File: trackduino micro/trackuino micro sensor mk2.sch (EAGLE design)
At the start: 42 parts, among them IC2 74AHC1G125DBV, SW1 SPST_TACT-KMR2, U1 ATMEGA168MLF, Y1 16MHZ

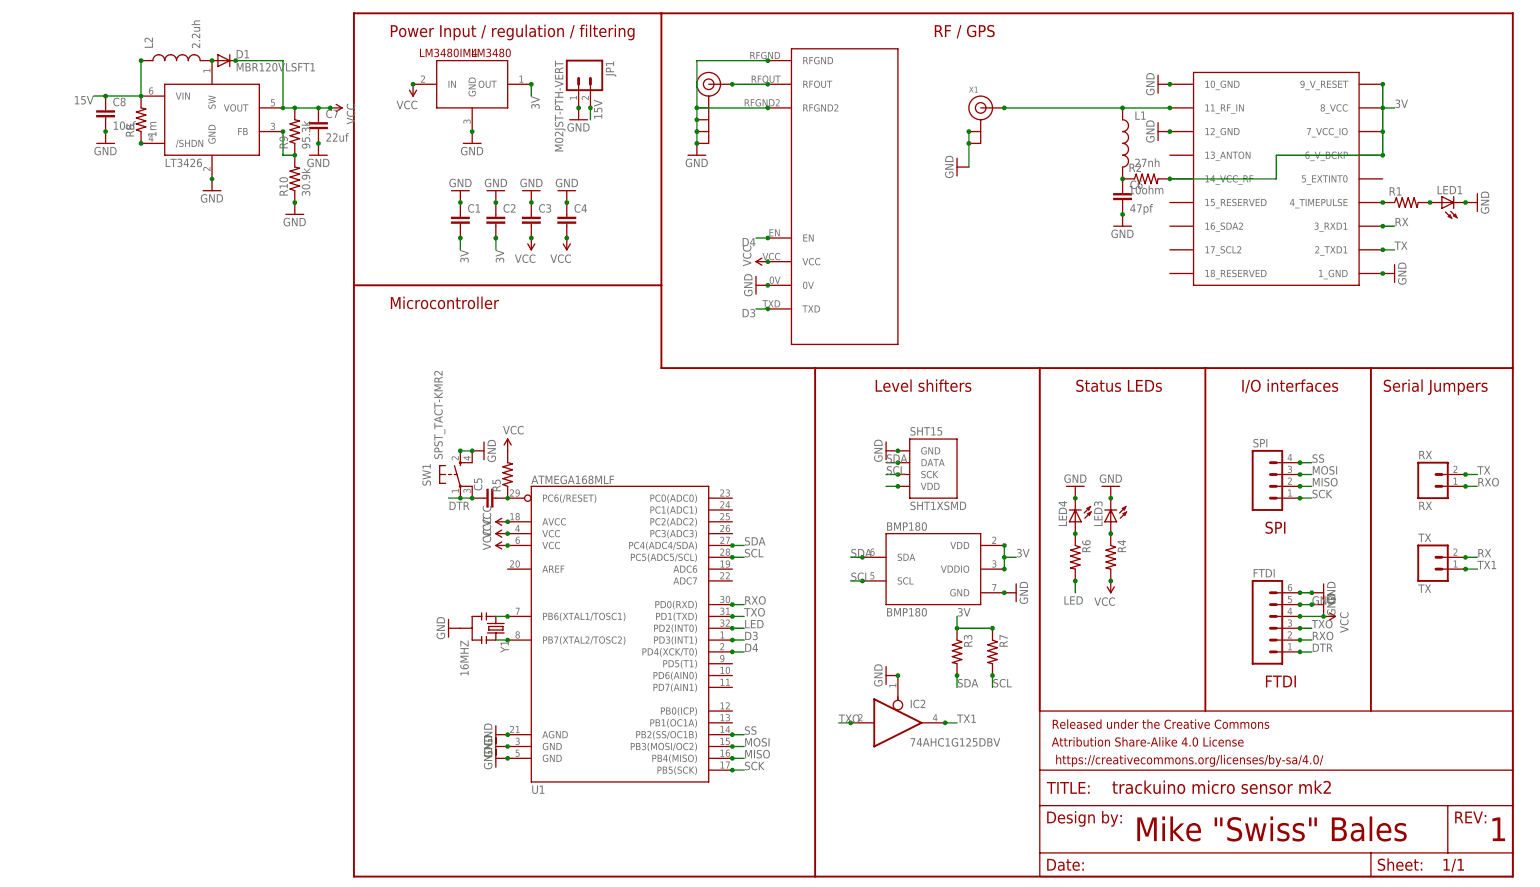
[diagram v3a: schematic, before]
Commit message: added part values
added part values to the schematic.
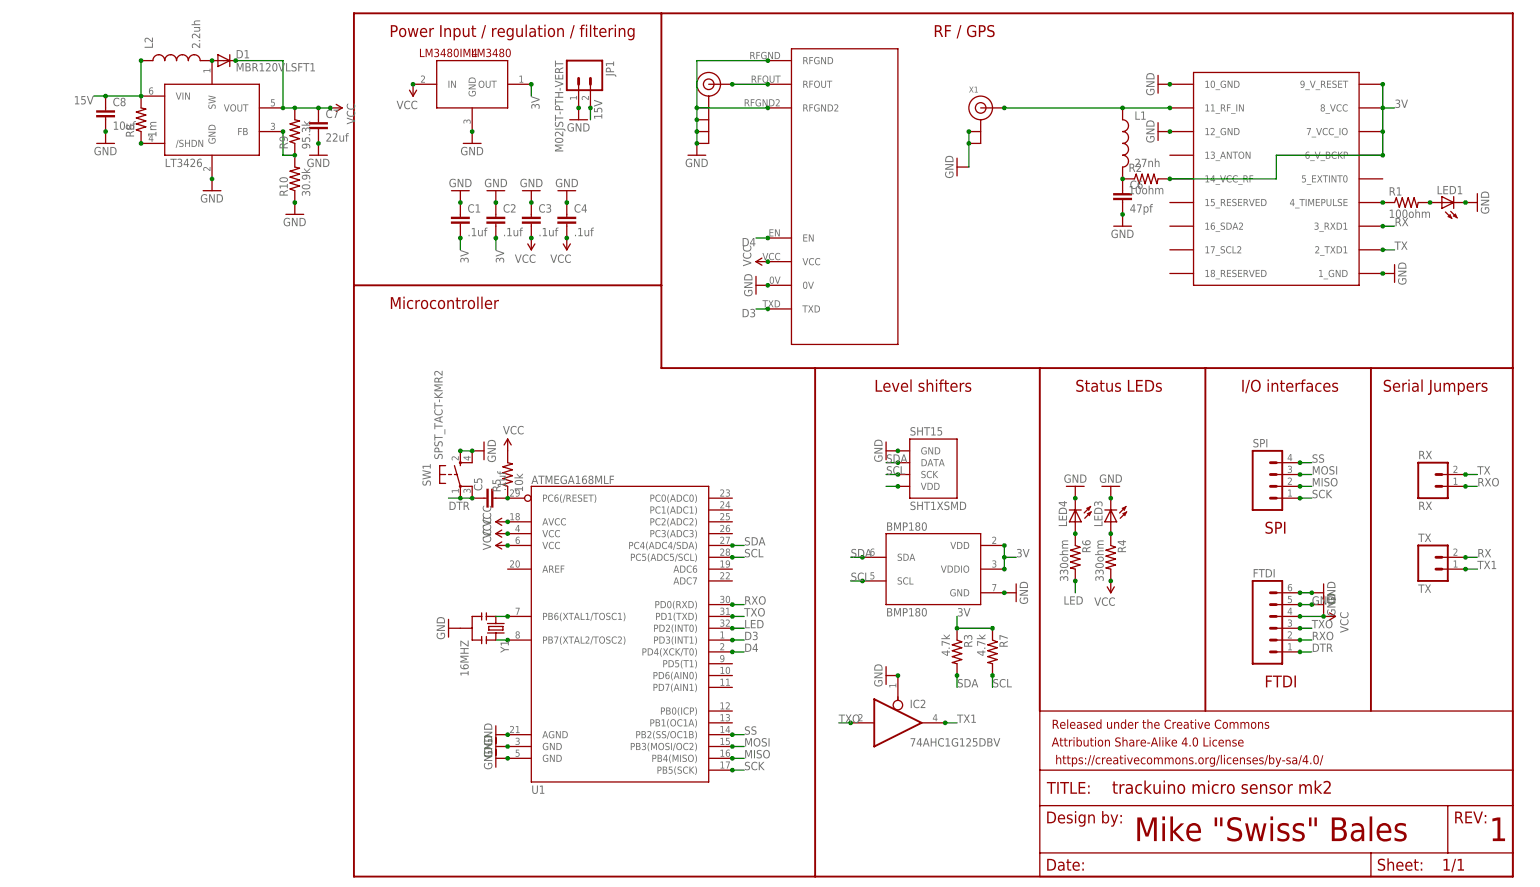
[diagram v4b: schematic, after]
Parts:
- C1, C2, C3, C4, C5: value (none) -> .1uf
- R1: value (none) -> 100ohm
- R3, R7: value (none) -> 4.7k
- R4, R6: value (none) -> 330ohm
- R5: value (none) -> 10k
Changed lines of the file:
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@@
 <part name="SUPPLY3" library="SparkFun-Aesthetics" deviceset="VCC" device=""/>
 <part name="GND7" library="SparkFun-Aesthetics" deviceset="GND" device=""/>
-<part name="R1" library="SparkFun-Resistors" deviceset="RESISTOR" device="0805-RES"/>
+<part name="R1" library="SparkFun-Resistors" deviceset="RESISTOR" device="0805-RES" value="100ohm"/>
 <part name="LED1" library="adafruit" deviceset="LED" device="CHIP-LED0805"/>
 <part name="GND8" library="SparkFun-Aesthetics" deviceset="GND" device=""/>
@@
 <part name="GND13" library="SparkFun-Aesthetics" deviceset="GND" device=""/>
 <part name="GND14" library="SparkFun-Aesthetics" deviceset="GND" device=""/>
-<part name="C1" library="SparkFun-Capacitors" deviceset="CAP" device="0805"/>
-<part name="C2" library="SparkFun-Capacitors" deviceset="CAP" device="0805"/>
-<part name="C3" library="SparkFun-Capacitors" deviceset="CAP" device="0805"/>
-<part name="C4" library="SparkFun-Capacitors" deviceset="CAP" device="0805"/>
+<part name="C1" library="SparkFun-Capacitors" deviceset="CAP" device="0805" value=".1uf"/>
+<part name="C2" library="SparkFun-Capacitors" deviceset="CAP" device="0805" value=".1uf"/>
+<part name="C3" library="SparkFun-Capacitors" deviceset="CAP" device="0805" value=".1uf"/>
+<part name="C4" library="SparkFun-Capacitors" deviceset="CAP" device="0805" value=".1uf"/>
 <part name="GND15" library="SparkFun-Aesthetics" deviceset="GND" device=""/>
 <part name="GND17" library="SparkFun-Aesthetics" deviceset="GND" device=""/>
@@
 <part name="SUPPLY5" library="SparkFun-Aesthetics" deviceset="VCC" device=""/>
 <part name="LED3" library="adafruit" deviceset="LED" device="CHIP-LED0805"/>
-<part name="R4" library="SparkFun-Resistors" deviceset="RESISTOR" device="0805-RES"/>
+<part name="R4" library="SparkFun-Resistors" deviceset="RESISTOR" device="0805-RES" value="330ohm"/>
 <part name="GND19" library="SparkFun-Aesthetics" deviceset="GND" device=""/>
 <part name="SUPPLY6" library="SparkFun-Aesthetics" deviceset="VCC" device=""/>
@@
 <part name="GND22" library="SparkFun-Aesthetics" deviceset="GND" device=""/>
 <part name="SUPPLY9" library="SparkFun-Aesthetics" deviceset="VCC" device=""/>
-<part name="R5" library="SparkFun-Resistors" deviceset="RESISTOR" device="0805-RES"/>
+<part name="R5" library="SparkFun-Resistors" deviceset="RESISTOR" device="0805-RES" value="10k"/>
 <part name="SUPPLY10" library="SparkFun-Aesthetics" deviceset="VCC" device=""/>
-<part name="C5" library="SparkFun-Capacitors" deviceset="CAP" device="0805"/>
+<part name="C5" library="SparkFun-Capacitors" deviceset="CAP" device="0805" value=".1uf"/>
 <part name="TX" library="SparkFun-Connectors" deviceset="M02" device="PTH" value="TX"/>
 <part name="SPI" library="SparkFun-Connectors" deviceset="M04" device="1X04_NO_SILK"/>
@@
 <part name="GND25" library="SparkFun-Aesthetics" deviceset="GND" device=""/>
 <part name="LED4" library="adafruit" deviceset="LED" device="CHIP-LED0805"/>
-<part name="R6" library="SparkFun-Resistors" deviceset="RESISTOR" device="0805-RES"/>
+<part name="R6" library="SparkFun-Resistors" deviceset="RESISTOR" device="0805-RES" value="330ohm"/>
 <part name="GND26" library="SparkFun-Aesthetics" deviceset="GND" device=""/>
 <part name="GND24" library="SparkFun-Aesthetics" deviceset="GND" device=""/>
@@
 <part name="GND16" library="SparkFun-Aesthetics" deviceset="GND" device=""/>
 <part name="GND20" library="SparkFun-Aesthetics" deviceset="GND" device=""/>
-<part name="R3" library="SparkFun-Resistors" deviceset="RESISTOR" device="0805-RES"/>
-<part name="R7" library="SparkFun-Resistors" deviceset="RESISTOR" device="0805-RES"/>
+<part name="R3" library="SparkFun-Resistors" deviceset="RESISTOR" device="0805-RES" value="4.7k"/>
+<part name="R7" library="SparkFun-Resistors" deviceset="RESISTOR" device="0805-RES" value="4.7k"/>
 <part name="GND27" library="SparkFun-Aesthetics" deviceset="GND" device=""/>
 <part name="SUPPLY1" library="SparkFun-Aesthetics" deviceset="VCC" device=""/>

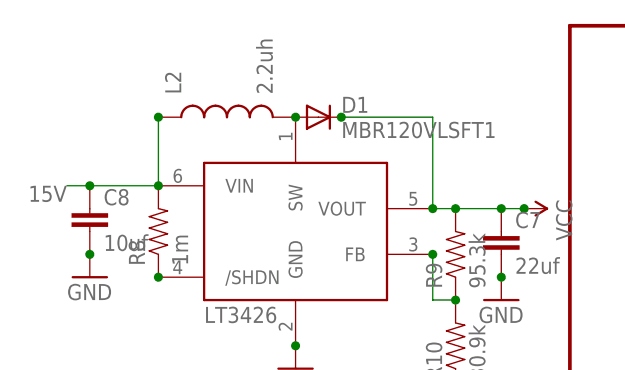
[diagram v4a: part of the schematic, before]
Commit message: replaced inductor
the 0805 inductor was getting way too hot due to being run well beyond
saturation. replaced with a 1812 inductor
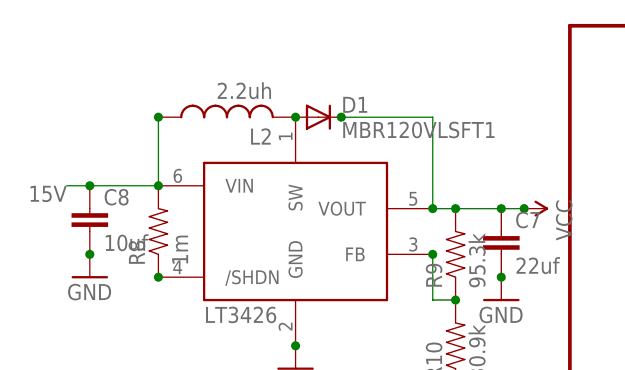
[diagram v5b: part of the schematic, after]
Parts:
- L2: device SparkFun-Passives:INDUCTOR0805 -> resistor:L-USL1812
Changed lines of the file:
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@@
 <?xml version="1.0" encoding="utf-8"?>
 <!DOCTYPE eagle SYSTEM "eagle.dtd">
-<eagle version="7.1.0">
+<eagle version="7.2.0">
 <drawing>
 <settings>
@@
 <part name="LT3426" library="adafruit" deviceset="LT3426" device=""/>
 <part name="D1" library="diode" deviceset="DIODE-" device="SOD123" value="MBR120VLSFT1"/>
-<part name="L2" library="SparkFun-Passives" deviceset="INDUCTOR" device="0805" value="2.2uh"/>
+<part name="L2" library="resistor" deviceset="L-US" device="L1812" value="2.2uh"/>
 <part name="R8" library="SparkFun-Resistors" deviceset="RESISTOR" device="0805-RES" value="1m"/>
 <part name="R9" library="SparkFun-Resistors" deviceset="RESISTOR" device="0805-RES" value="95.3k"/>

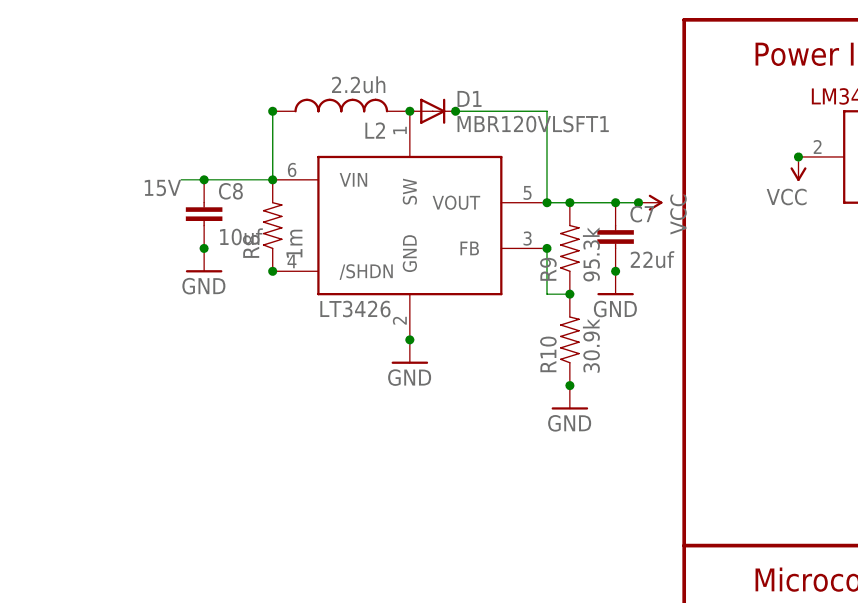
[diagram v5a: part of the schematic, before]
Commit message: added output cap
added a larger value output cap
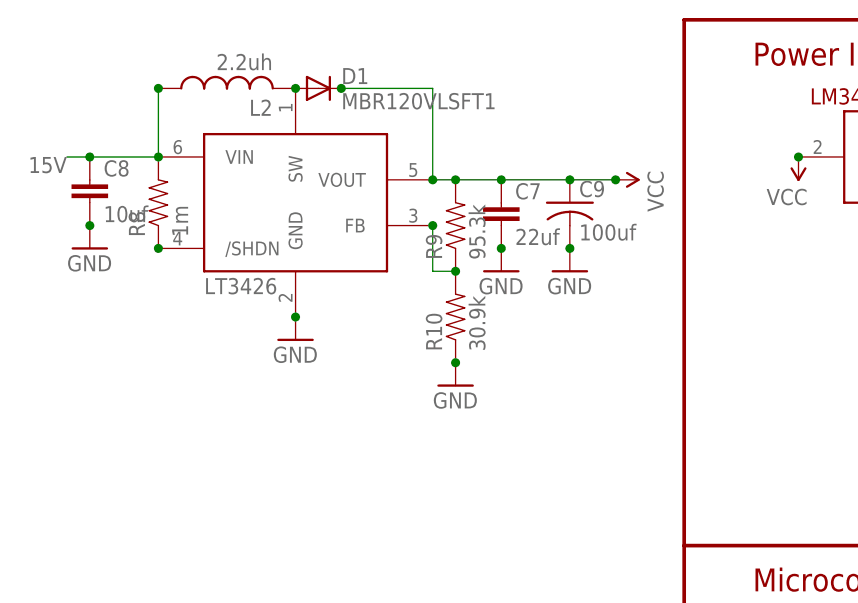
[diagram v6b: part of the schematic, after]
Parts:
- added C9: 100uf, resistor:C-USC1206
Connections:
- net GND: now also C9.2
- net VCC: now also C9.1
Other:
- moved on the sheet: C7, C8, D1, L2, R10, R8, R9
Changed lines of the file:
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@@
 <part name="GND29" library="SparkFun-Aesthetics" deviceset="GND" device=""/>
 <part name="GND30" library="SparkFun-Aesthetics" deviceset="GND" device=""/>
+<part name="C9" library="resistor" deviceset="C-US" device="C1206" value="100uf"/>
+<part name="GND31" library="SparkFun-Aesthetics" deviceset="GND" device=""/>
 </parts>
 <sheets>
@@
 <instance part="R3" gate="G$1" x="129.54" y="48.26" rot="R270"/>
 <instance part="R7" gate="G$1" x="137.16" y="48.26" rot="R270"/>
-<instance part="GND27" gate="1" x="-30.48" y="147.32"/>
-<instance part="SUPPLY1" gate="G$1" x="-5.08" y="165.1" rot="R270"/>
-<instance part="LT3426" gate="G$1" x="-30.48" y="162.56"/>
-<instance part="D1" gate="G$1" x="-27.94" y="175.26"/>
-<instance part="L2" gate="G$1" x="-38.1" y="175.26" rot="R90"/>
-<instance part="R8" gate="G$1" x="-45.72" y="162.56" rot="R90"/>
-<instance part="R9" gate="G$1" x="-12.7" y="160.02" rot="R90"/>
-<instance part="R10" gate="G$1" x="-12.7" y="149.86" rot="R90"/>
-<instance part="GND28" gate="1" x="-12.7" y="142.24"/>
-<instance part="C7" gate="G$1" x="-7.62" y="160.02"/>
-<instance part="C8" gate="G$1" x="-53.34" y="162.56"/>
-<instance part="GND29" gate="1" x="-53.34" y="157.48"/>
-<instance part="GND30" gate="1" x="-7.62" y="154.94"/>
+<instance part="GND27" gate="1" x="-43.18" y="149.86"/>
+<instance part="SUPPLY1" gate="G$1" x="-7.62" y="167.64" rot="R270"/>
+<instance part="LT3426" gate="G$1" x="-43.18" y="165.1"/>
+<instance part="D1" gate="G$1" x="-40.64" y="177.8"/>
+<instance part="L2" gate="G$1" x="-50.8" y="177.8" rot="R90"/>
+<instance part="R8" gate="G$1" x="-58.42" y="165.1" rot="R90"/>
+<instance part="R9" gate="G$1" x="-25.4" y="162.56" rot="R90"/>
+<instance part="R10" gate="G$1" x="-25.4" y="152.4" rot="R90"/>
+<instance part="GND28" gate="1" x="-25.4" y="144.78"/>
+<instance part="C7" gate="G$1" x="-20.32" y="162.56"/>
+<instance part="C8" gate="G$1" x="-66.04" y="165.1"/>
+<instance part="GND29" gate="1" x="-66.04" y="160.02"/>
+<instance part="GND30" gate="1" x="-20.32" y="157.48"/>
+<instance part="C9" gate="G$1" x="-12.7" y="165.1"/>
+<instance part="GND31" gate="1" x="-12.7" y="157.48"/>
 </instances>
 <busses>
@@
 <pinref part="LT3426" gate="G$1" pin="GND"/>
 <pinref part="GND27" gate="1" pin="GND"/>
-<junction x="-30.48" y="149.86"/>
+<junction x="-43.18" y="152.4"/>
 </segment>
 <segment>
 <pinref part="R10" gate="G$1" pin="1"/>
 <pinref part="GND28" gate="1" pin="GND"/>
-<junction x="-12.7" y="144.78"/>
+<junction x="-25.4" y="147.32"/>
 </segment>
 <segment>
 <pinref part="C8" gate="G$1" pin="2"/>
 <pinref part="GND29" gate="1" pin="GND"/>
-<junction x="-53.34" y="160.02"/>
+<junction x="-66.04" y="162.56"/>
 </segment>
 <segment>
 <pinref part="C7" gate="G$1" pin="2"/>
 <pinref part="GND30" gate="1" pin="GND"/>
-<junction x="-7.62" y="157.48"/>
+<junction x="-20.32" y="160.02"/>
+</segment>
+<segment>
+<pinref part="C9" gate="G$1" pin="2"/>
+<pinref part="GND31" gate="1" pin="GND"/>
+<junction x="-12.7" y="160.02"/>
 </segment>
 </net>
@@
 <pinref part="LT3426" gate="G$1" pin="VOUT"/>
 <pinref part="SUPPLY1" gate="G$1" pin="VCC"/>
-<wire x1="-5.08" y1="165.1" x2="-7.62" y2="165.1" width="0.1524" layer="91"/>
+<wire x1="-7.62" y1="167.64" x2="-12.7" y2="167.64" width="0.1524" layer="91"/>
 <pinref part="D1" gate="G$1" pin="C"/>
-<wire x1="-7.62" y1="165.1" x2="-12.7" y2="165.1" width="0.1524" layer="91"/>
-<wire x1="-12.7" y1="165.1" x2="-15.24" y2="165.1" width="0.1524" layer="91"/>
-<wire x1="-25.4" y1="175.26" x2="-15.24" y2="175.26" width="0.1524" layer="91"/>
-<wire x1="-15.24" y1="175.26" x2="-15.24" y2="165.1" width="0.1524" layer="91"/>
+<wire x1="-12.7" y1="167.64" x2="-20.32" y2="167.64" width="0.1524" layer="91"/>
+<wire x1="-20.32" y1="167.64" x2="-25.4" y2="167.64" width="0.1524" layer="91"/>
+<wire x1="-25.4" y1="167.64" x2="-27.94" y2="167.64" width="0.1524" layer="91"/>
+<wire x1="-38.1" y1="177.8" x2="-27.94" y2="177.8" width="0.1524" layer="91"/>
+<wire x1="-27.94" y1="177.8" x2="-27.94" y2="167.64" width="0.1524" layer="91"/>
 <pinref part="R9" gate="G$1" pin="2"/>
-<junction x="-12.7" y="165.1"/>
-<junction x="-15.24" y="165.1"/>
-<junction x="-25.4" y="175.26"/>
+<junction x="-25.4" y="167.64"/>
+<junction x="-27.94" y="167.64"/>
+<junction x="-38.1" y="177.8"/>
 <pinref part="C7" gate="G$1" pin="1"/>
-<junction x="-7.62" y="165.1"/>
-<junction x="-5.08" y="165.1"/>
+<junction x="-20.32" y="167.64"/>
+<junction x="-7.62" y="167.64"/>
+<pinref part="C9" gate="G$1" pin="1"/>
+<junction x="-12.7" y="167.64"/>
 </segment>
 </net>
@@
 <net name="15V" class="0">
 <segment>
-<wire x1="-45.72" y1="167.64" x2="-53.34" y2="167.64" width="0.1524" layer="91"/>
-<label x="-55.88" y="167.64" size="1.778" layer="95" rot="R180"/>
+<wire x1="-58.42" y1="170.18" x2="-66.04" y2="170.18" width="0.1524" layer="91"/>
+<label x="-68.58" y="170.18" size="1.778" layer="95" rot="R180"/>
 <pinref part="LT3426" gate="G$1" pin="VIN"/>
-<junction x="-45.72" y="167.64"/>
+<junction x="-58.42" y="170.18"/>
 <pinref part="L2" gate="G$1" pin="1"/>
-<wire x1="-53.34" y1="167.64" x2="-55.88" y2="167.64" width="0.1524" layer="91"/>
-<wire x1="-45.72" y1="175.26" x2="-45.72" y2="167.64" width="0.1524" layer="91"/>
-<junction x="-45.72" y="175.26"/>
+<wire x1="-66.04" y1="170.18" x2="-68.58" y2="170.18" width="0.1524" layer="91"/>
+<wire x1="-58.42" y1="177.8" x2="-58.42" y2="170.18" width="0.1524" layer="91"/>
+<junction x="-58.42" y="177.8"/>
 <pinref part="R8" gate="G$1" pin="2"/>
 <pinref part="C8" gate="G$1" pin="1"/>
-<junction x="-53.34" y="167.64"/>
+<junction x="-66.04" y="170.18"/>
 </segment>
 <segment>
@@
 <pinref part="D1" gate="G$1" pin="A"/>
 <pinref part="L2" gate="G$1" pin="2"/>
-<junction x="-30.48" y="175.26"/>
+<junction x="-43.18" y="177.8"/>
 <pinref part="L2" gate="G$1" pin="2"/>
 </segment>
@@
 <pinref part="LT3426" gate="G$1" pin="/SHDN"/>
 <pinref part="R8" gate="G$1" pin="1"/>
-<junction x="-45.72" y="157.48"/>
+<junction x="-58.42" y="160.02"/>
 </segment>
 </net>
@@
 <pinref part="R10" gate="G$1" pin="2"/>
 <pinref part="LT3426" gate="G$1" pin="FB"/>
-<wire x1="-15.24" y1="160.02" x2="-15.24" y2="154.94" width="0.1524" layer="91"/>
-<wire x1="-15.24" y1="154.94" x2="-12.7" y2="154.94" width="0.1524" layer="91"/>
-<junction x="-12.7" y="154.94"/>
-<junction x="-15.24" y="160.02"/>
-</segment>
-</net>
+<wire x1="-27.94" y1="162.56" x2="-27.94" y2="157.48" width="0.1524" layer="91"/>
+<wire x1="-27.94" y1="157.48" x2="-25.4" y2="157.48" width="0.1524" layer="91"/>
+<junction x="-25.4" y="157.48"/>
+<junction x="-27.94" y="162.56"/>
+</segment>
+</net>

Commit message: firmware
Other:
- note added: "Sensors"
- moved on the sheet: C1, C2, C3, C4, C5, C7, C8, C9, D1, IC2, JP1, L2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
